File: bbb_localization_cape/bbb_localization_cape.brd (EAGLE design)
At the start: 86.4 x 54.6 mm, 32 parts, among them J1 CONN_04, J2 MOLEX-22-03-5035, U1 SN65HVD256DR, U2 ARDUCAMOV5642, U3 MSP430G2553IPW20R, U4 SN74LV1T126DCKR, U5 SN74LV1T125DCKR, U6 SN74LV1T126DCKR, U7 LP38693MP-3.3/NOPB, U8 LM1085ISX-ADJ

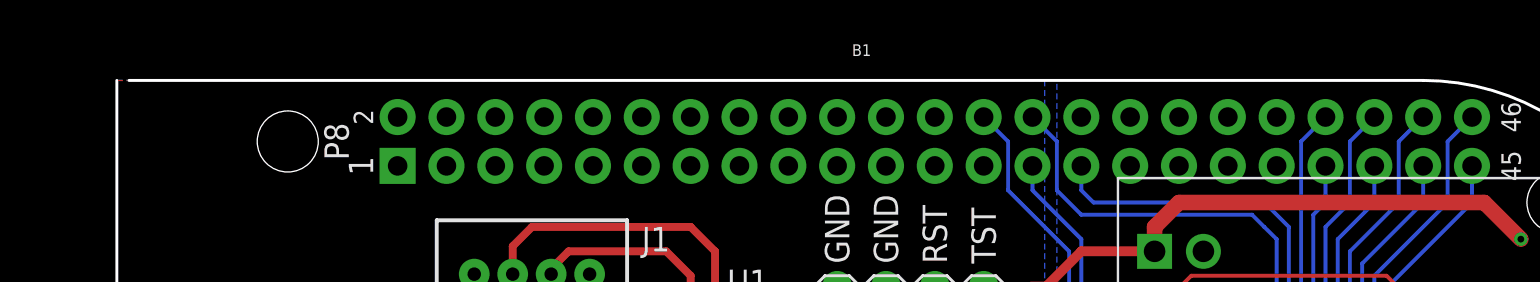
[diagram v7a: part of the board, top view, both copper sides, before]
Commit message: Added dimension layer
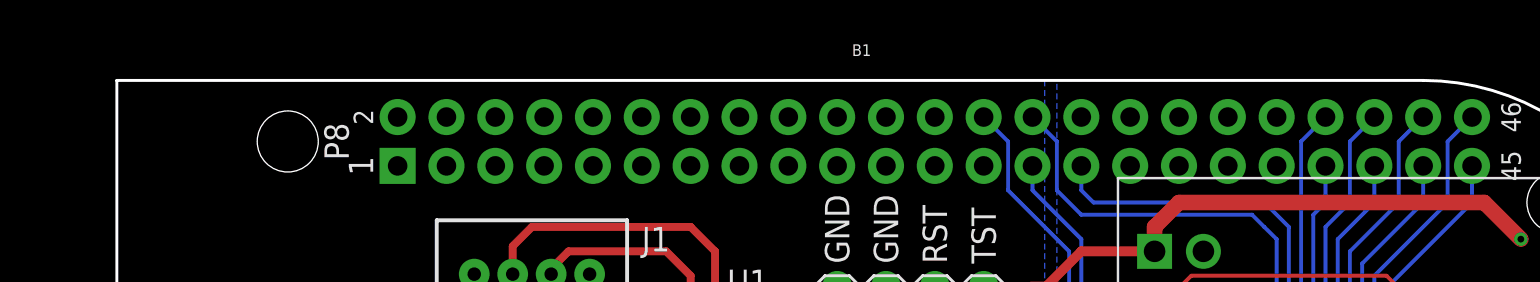
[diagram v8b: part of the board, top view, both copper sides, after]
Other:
- outline, holes or cut-outs redrawn
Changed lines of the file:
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@@
 <wire x1="85.09" y1="12.7" x2="85.09" y2="41.91" width="0.1524" layer="20"/>
 <wire x1="85.09" y1="41.91" x2="72.39" y2="54.61" width="0.1524" layer="20" curve="90"/>
-<wire x1="72.39" y1="54.61" x2="5.08" y2="54.61" width="0.1524" layer="20"/>
+<wire x1="72.39" y1="54.61" x2="4.445" y2="54.61" width="0.1524" layer="20"/>
 </plain>
 <attributes>
@@
 <contactref element="B1" pad="P9.44"/>
 <contactref element="B1" pad="P9.46"/>
+<wire x1="35.8648" y1="6.97" x2="31.75" y2="20.635" width="0" layer="19" extent="1-1"/>
 </signal>
 <signal name="+5V">
